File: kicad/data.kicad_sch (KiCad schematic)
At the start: 39 parts, among them U7 86C325

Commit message: some optimizations and silkscreen updating
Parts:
- R5: value 2 x 33R -> 33R
- R5: value 10K each -> 10K
- R5: value 3 x 33R -> 33R
- U3, U4, U5, U6: value ~ -> V53C16258H
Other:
- note removed: "Default OFF"
- note removed: "PD16 = R45 PD17 = R46"
- note removed: "PD5 = R40 PD6 = R41 PD7 = R42"
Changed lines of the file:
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@@
     (effects (font (size 1.27 1.27)) (justify left bottom))
   )
-  (text "Default OFF" (at 194.31 142.24 0)
-    (effects (font (size 1.27 1.27) bold) (justify left bottom))
-  )
   (text "Serial Port I/O Address & Type Select" (at 217.17 78.74 0)
     (effects (font (size 1.27 1.27)) (justify left bottom))
@@
     (effects (font (size 1.27 1.27)) (justify left bottom))
   )
-  (text "PD16 = R45\nPD17 = R46" (at 241.3 27.94 0)
-    (effects (font (size 1.27 1.27) (thickness 0.254) bold) (justify left bottom))
-  )
   (text "0N = VL Bus" (at 190.5 34.29 0)
     (effects (font (size 1.27 1.27)) (justify left bottom))
@@
     (effects (font (size 1.27 1.27)) (justify left bottom))
   )
-  (text "PD5 = R40\nPD6 = R41\nPD7 = R42" (at 199.39 90.17 0)
-    (effects (font (size 1.27 1.27) bold) (justify left bottom))
-  )
   (text "Display Memory Size" (at 157.48 85.09 0)
     (effects (font (size 1.27 1.27)) (justify left bottom))
@@
     (effects (font (size 1.27 1.27) bold) (justify left bottom))
   )
-  (text "Default OFF" (at 194.31 81.28 0)
-    (effects (font (size 1.27 1.27) bold) (justify left bottom))
-  )
   (text "~{CAS}/~{OE} Adjust" (at 217.17 25.4 0)
     (effects (font (size 1.27 1.27)) (justify left bottom))
@@
     (effects (font (size 1.27 1.27)) (justify left bottom))
   )
-  (text "Default OFF" (at 194.31 120.65 0)
-    (effects (font (size 1.27 1.27) bold) (justify left bottom))
-  )
   (text "0N = 64-KByte video BIOS\nOFF = 32-KByte video BIOS"
     (at 181.61 116.84 0)
@@
       (effects (font (size 1.27 1.27)))
     )
-    (property "Value" "~" (at 132.08 86.36 0)
-      (effects (font (size 1.27 1.27)))
+    (property "Value" "V53C16258H" (at 132.08 86.36 0)
+      (effects (font (size 1.27 1.27)) hide)
     )
     (property "Footprint" "VLB:SOJ-40_10.16x26.00mm_P1.27mm" (at 132.08 86.36 0)
@@
       (effects (font (size 1.27 1.27)))
     )
-    (property "Value" "~" (at 95.25 86.36 0)
-      (effects (font (size 1.27 1.27)))
+    (property "Value" "V53C16258H" (at 95.25 86.36 0)
+      (effects (font (size 1.27 1.27)) hide)
     )
     (property "Footprint" "VLB:SOJ-40_10.16x26.00mm_P1.27mm" (at 95.25 86.36 0)
@@
       (effects (font (size 1.27 1.27)) (justify left))
     )
-    (property "Value" "2 x 33R" (at 40.64 180.34 90)
+    (property "Value" "33R" (at 40.64 180.34 90)
       (effects (font (size 1.27 1.27)) (justify left) hide)
     )
@@
       (effects (font (size 1.27 1.27)))
     )
-    (property "Value" "~" (at 95.25 27.94 0)
-      (effects (font (size 1.27 1.27)))
+    (property "Value" "V53C16258H" (at 95.25 27.94 0)
+      (effects (font (size 1.27 1.27)) hide)
     )
     (property "Footprint" "VLB:SOJ-40_10.16x26.00mm_P1.27mm" (at 95.25 27.94 0)
@@
       (effects (font (size 1.27 1.27)) (justify left))
     )
-    (property "Value" "10K each" (at 250.19 132.08 90)
+    (property "Value" "10K" (at 250.19 132.08 90)
       (effects (font (size 1.27 1.27)) (justify left))
     )
@@
       (effects (font (size 1.27 1.27)) (justify left))
     )
-    (property "Value" "3 x 33R" (at 40.64 170.18 90)
+    (property "Value" "33R" (at 40.64 170.18 90)
       (effects (font (size 1.27 1.27)) (justify left) hide)
     )
@@
       (effects (font (size 1.27 1.27)))
     )
-    (property "Value" "~" (at 132.08 27.94 0)
-      (effects (font (size 1.27 1.27)))
+    (property "Value" "V53C16258H" (at 132.08 27.94 0)
+      (effects (font (size 1.27 1.27)) hide)
     )
     (property "Footprint" "VLB:SOJ-40_10.16x26.00mm_P1.27mm" (at 132.08 27.94 0)

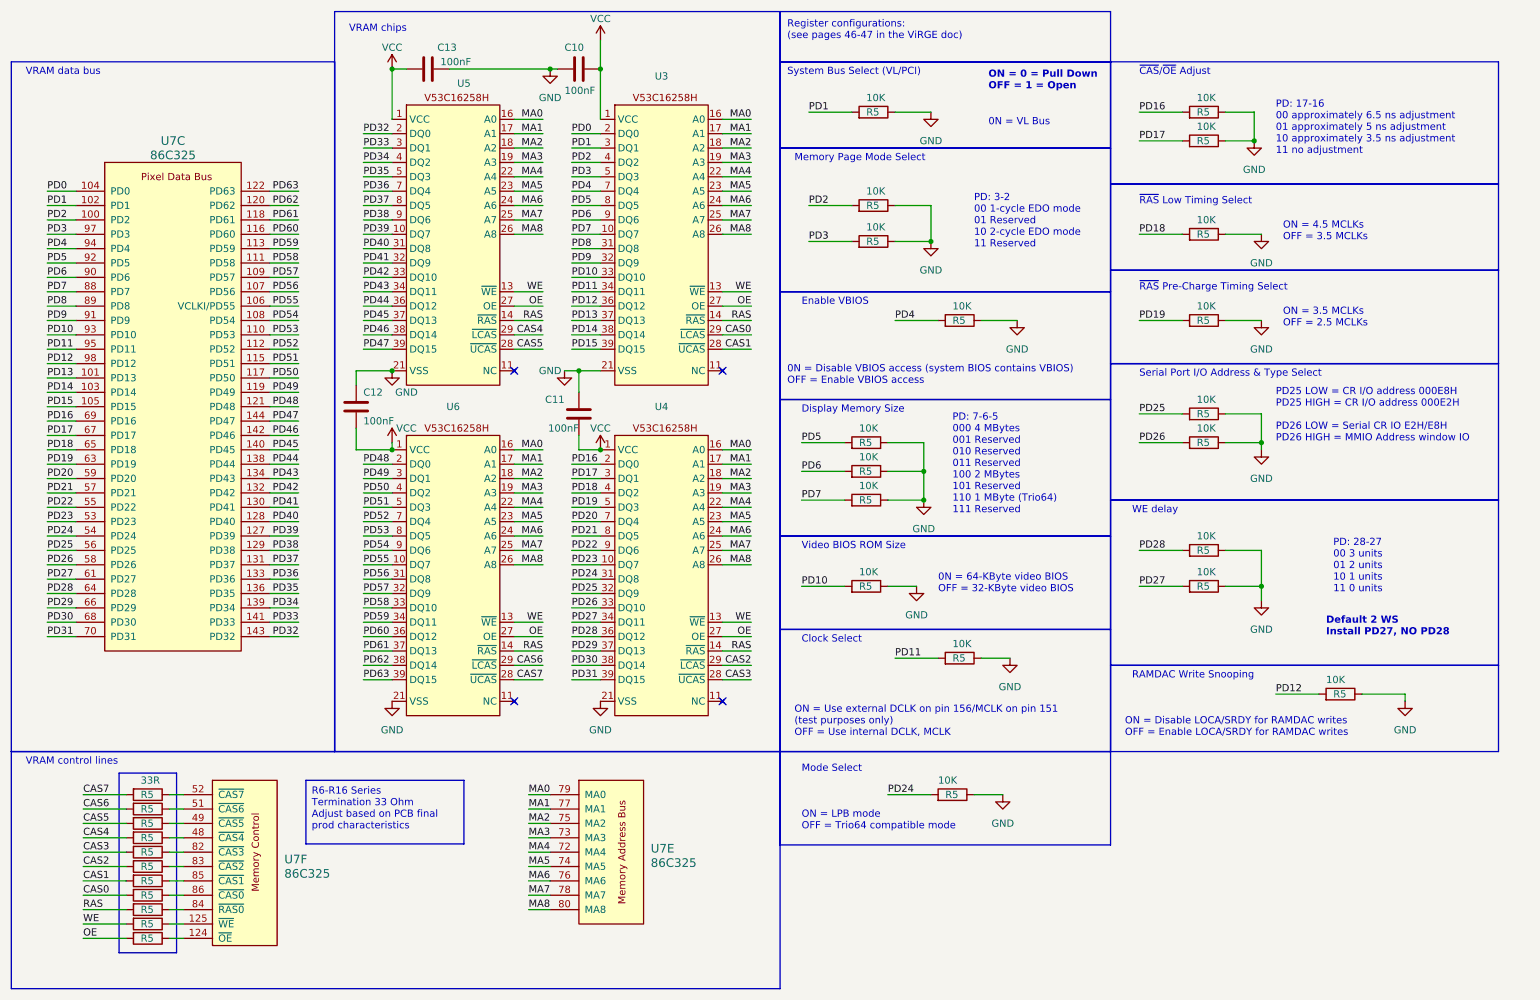
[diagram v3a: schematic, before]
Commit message: updated VLB footprint
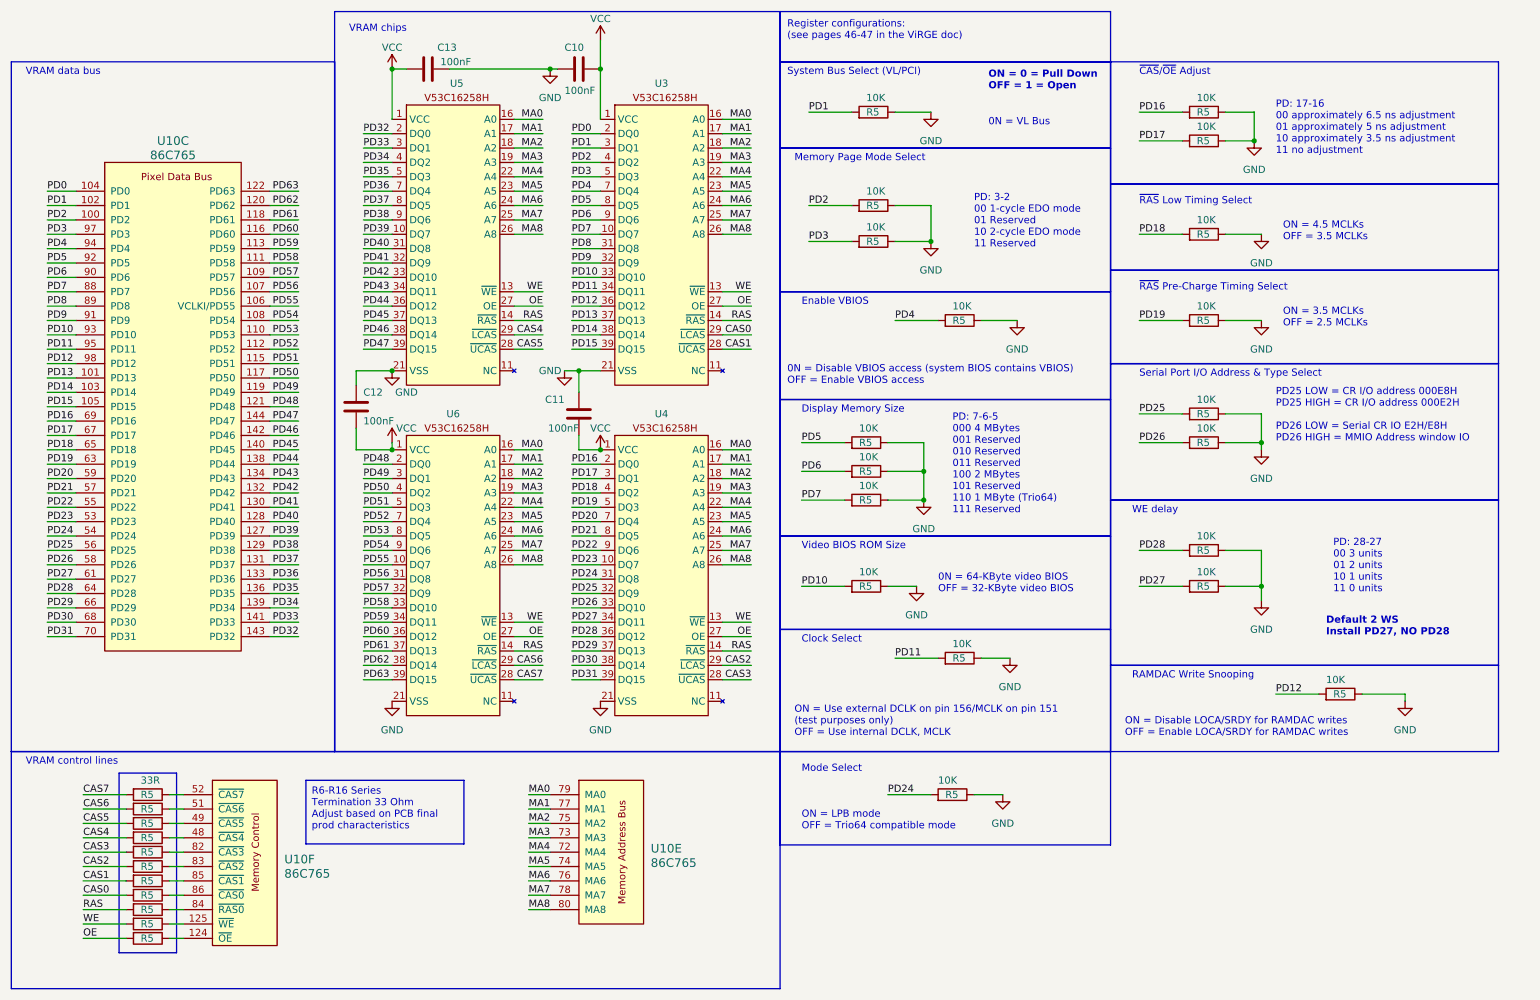
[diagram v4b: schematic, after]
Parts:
- removed U7: 86C325, VLB:QFP-208, symbol virge:86C375
- added U10: 86C765, Package_QFP:PQFP-208_28x28mm_P0.5mm, symbol virge:86C765
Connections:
- net MA0: now also U10.79 (MA0)
- net MA1: now also U10.77 (MA1)
- net MA2: now also U10.75 (MA2)
- net MA3: now also U10.73 (MA3)
- net MA4: now also U10.72 (MA4)
- net MA5: now also U10.74 (MA5)
- net MA6: now also U10.76 (MA6)
- net MA7: now also U10.78 (MA7)
- net MA8: now also U10.80 (MA8)
- net PD0: now also U10.104 (PD0)
- net PD1: now also U10.102 (PD1)
- net PD10: now also U10.93 (PD10)
- net PD11: now also U10.95 (PD11)
- net PD12: now also U10.98 (PD12)
- net PD13: now also U10.101 (PD13)
- net PD14: now also U10.103 (PD14)
- net PD15: now also U10.105 (PD15)
- net PD16: now also U10.69 (PD16)
- net PD17: now also U10.67 (PD17)
- net PD18: now also U10.65 (PD18)
- net PD19: now also U10.63 (PD19)
- net PD2: now also U10.100 (PD2)
- net PD20: now also U10.59 (PD20)
- net PD21: now also U10.57 (PD21)
- net PD22: now also U10.55 (PD22)
- net PD23: now also U10.53 (PD23)
- net PD24: now also U10.54 (PD24)
- net PD25: now also U10.56 (PD25)
- net PD26: now also U10.58 (PD26)
- net PD27: now also U10.61 (PD27)
- net PD28: now also U10.64 (PD28)
- net PD29: now also U10.66 (PD29)
- net PD3: now also U10.97 (PD3)
- net PD30: now also U10.68 (PD30)
- net PD31: now also U10.70 (PD31)
- net PD32: now also U10.143 (PD32)
- net PD33: now also U10.141 (PD33)
- net PD34: now also U10.139 (PD34)
- net PD35: now also U10.136 (PD35)
- net PD36: now also U10.133 (PD36)
- net PD37: now also U10.131 (PD37)
- net PD38: now also U10.129 (PD38)
- net PD39: now also U10.127 (PD39)
- net PD4: now also U10.94 (PD4)
- net PD40: now also U10.128 (PD40)
- net PD41: now also U10.130 (PD41)
- net PD42: now also U10.132 (PD42)
- net PD43: now also U10.134 (PD43)
- net PD44: now also U10.138 (PD44)
- net PD45: now also U10.140 (PD45)
- net PD46: now also U10.142 (PD46)
- net PD47: now also U10.144 (PD47)
- net PD48: now also U10.121 (PD48)
- net PD49: now also U10.119 (PD49)
- net PD5: now also U10.92 (PD5)
- net PD50: now also U10.117 (PD50)
- net PD51: now also U10.115 (PD51)
- net PD52: now also U10.112 (PD52)
- net PD53: now also U10.110 (PD53)
- net PD54: now also U10.108 (PD54)
- net PD55: now also U10.106 (VCLKI/PD55)
- net PD56: now also U10.107 (PD56)
- net PD57: now also U10.109 (PD57)
- net PD58: now also U10.111 (PD58)
- net PD59: now also U10.113 (PD59)
- net PD6: now also U10.90 (PD6)
- net PD60: now also U10.116 (PD60)
- net PD61: now also U10.118 (PD61)
- net PD62: now also U10.120 (PD62)
- net PD63: now also U10.122 (PD63)
- net PD7: now also U10.88 (PD7)
- net PD8: now also U10.89 (PD8)
- net PD9: now also U10.91 (PD9)
- net at R5.1: now also U10.84 (~{RAS0})
- net at R5.1: now also U10.51 (~{CAS6})
- net at R5.1: now also U10.86 (~{CAS0})
- net at R5.1: now also U10.49 (~{CAS5})
- net at R5.1: now also U10.48 (~{CAS4})
- net at R5.1: now also U10.52 (~{CAS7})
- net at R5.1: now also U10.125 (~{WE})
- net at R5.1: now also U10.124 (~{OE})
- net at R5.1: now also U10.82 (~{CAS3})
- net at R5.1: now also U10.83 (~{CAS2})
- net at R5.1: now also U10.85 (~{CAS1})
- no-connect marks 4 -> 0

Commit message: fixed VGA footprint
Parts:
- U10: footprint Package_QFP:PQFP-208_28x28mm_P0.5mm -> VLB:QFP-208
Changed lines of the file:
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@@
       (effects (font (size 1.524 1.524)) (justify left))
     )
-    (property "Footprint" "Package_QFP:PQFP-208_28x28mm_P0.5mm" (at 19.05 158.75 0)
+    (property "Footprint" "VLB:QFP-208" (at 19.05 158.75 0)
       (effects (font (size 1.524 1.524)) (justify right) hide)
     )
@@
       (effects (font (size 1.524 1.524)) (justify left))
     )
-    (property "Footprint" "Package_QFP:PQFP-208_28x28mm_P0.5mm" (at 83.82 157.48 0)
+    (property "Footprint" "VLB:QFP-208" (at 83.82 157.48 0)
       (effects (font (size 1.524 1.524)) (justify right) hide)
     )
@@
       (effects (font (size 1.524 1.524)))
     )
-    (property "Footprint" "Package_QFP:PQFP-208_28x28mm_P0.5mm" (at 5.08 78.74 0)
-      (effects (font (size 1.524 1.524)) (justify right) hide)
-    )
+    (property "Footprint" "VLB:QFP-208" (at 5.08 78.74 0)
+      (effects (font (size 1.524 1.524)) (justify right) hide)
+    )

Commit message: updated to kicad 9
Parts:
- renumbered C10 to C16, C11 to C19, R5 to R10, R5 to R11, R5 to R12, R5 to R13, R5 to R14, R5 to R15, R5 to R16, R5 to R17, R5 to R18, R5 to R19, R5 to R23, R5 to R24, R5 to R25, R5 to R26, R5 to R27, R5 to R28, R5 to R29, R5 to R30, R5 to R31, R5 to R32, R5 to R33, R5 to R34, R5 to R35, R5 to R36, R5 to R37, R5 to R38, R5 to R39, R5 to R40, R5 to R41, R5 to R9, U10 to U7
